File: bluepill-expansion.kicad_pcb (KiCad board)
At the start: 2 copper layers, 90.9 x 73.2 mm, 39 parts, among them J1 SENSE_A, J10 ENCODERS, J11 LS2, J12 I/O 3V3, J13 DIGITAL_PWR, J2 SENSE_B, J3 POWER_DC, J4 MOTDC1, J5 MOTDC2, J6 I2C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

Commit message: cambiosEmma
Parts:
- removed C5, C7: 0.1uF, Capacitor_THT:C_Disc_D7.5mm_W2.5mm_P5.00mm
- added T1: miTornillo, miTornillo:M3, F.Cu at (189.1, 55.8)
- added T2: miTornillo, miTornillo:M3, F.Cu at (103.9, 123.1)
- added T3: miTornillo, miTornillo:M3, F.Cu at (104.1, 55.8)
- added T4: miTornillo, miTornillo:M3, F.Cu at (189.1, 123.1)
- moved J13 7.94 mm to (118.7, 58.4)
- moved J10 6.33 mm to (152.1, 58.3)
- moved J2 5.29 mm to (157.2, 61.7)
- moved R2 5.29 mm to (182.6, 60.5)
- moved J6 2.88 mm to (112.5, 119.4)
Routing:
- net VCC: track 123.3 -> 113.6 mm
- net ENC2_Q: track 28.8 -> 35.3 mm
- net GND: track 364.9 -> 359.5 mm
- net ENC2_D: track 31.0 -> 35.4 mm
- net ENC1_D: track 41.1 -> 45.1 mm
- net ENC1_Q: track 38.7 -> 42.0 mm
- net +5V: track 255.3 -> 252.2 mm, vias 2 -> 3
- net /PB5: track 72.9 -> 70.4 mm
- net ENA: track 22.8 -> 25.1 mm
- net SENSE_B: track 15.0 -> 12.7 mm
- net +3V3: track 87.8 -> 89.9 mm
- net SCL: track 13.5 -> 11.6 mm
- net SDA: track 13.5 -> 11.6 mm
- net UARTRX: track 22.7 -> 20.9 mm
- net MOT4: track 46.6 -> 45.2 mm
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
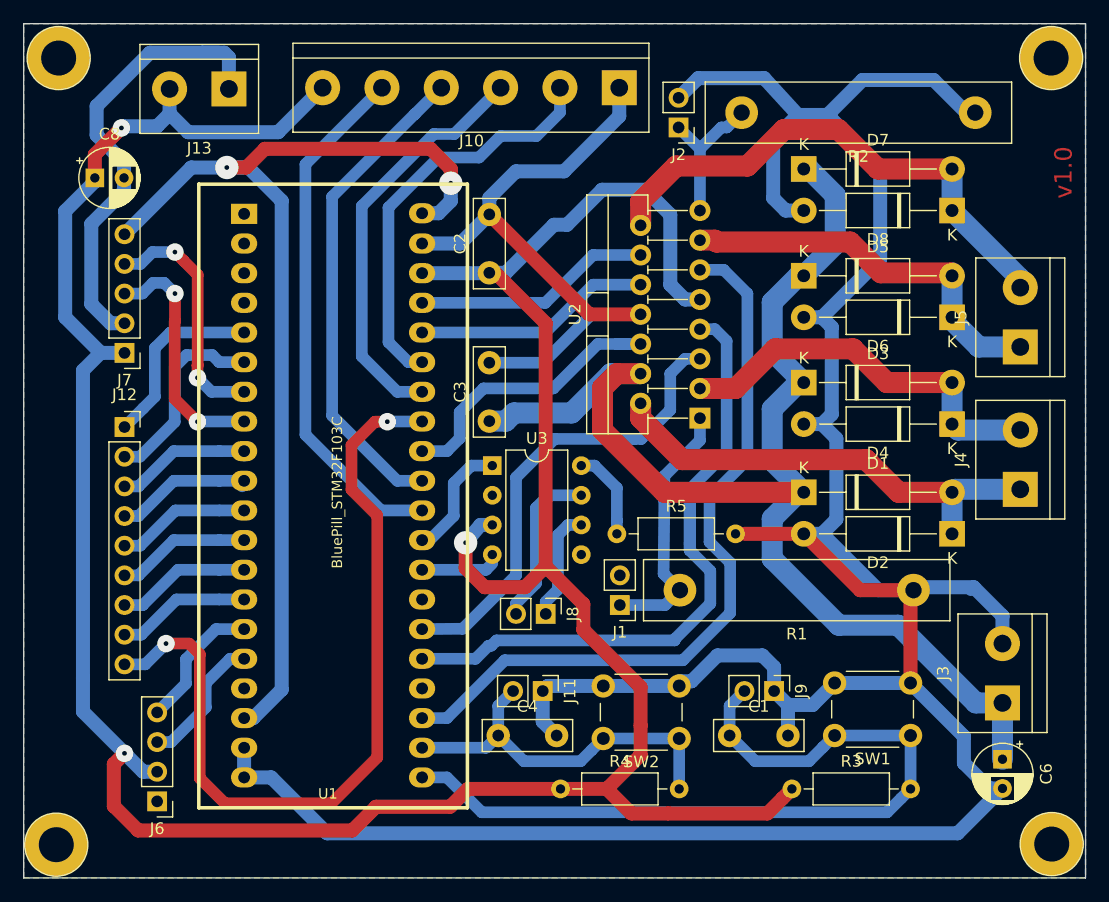
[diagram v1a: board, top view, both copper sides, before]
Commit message: CAN R 120
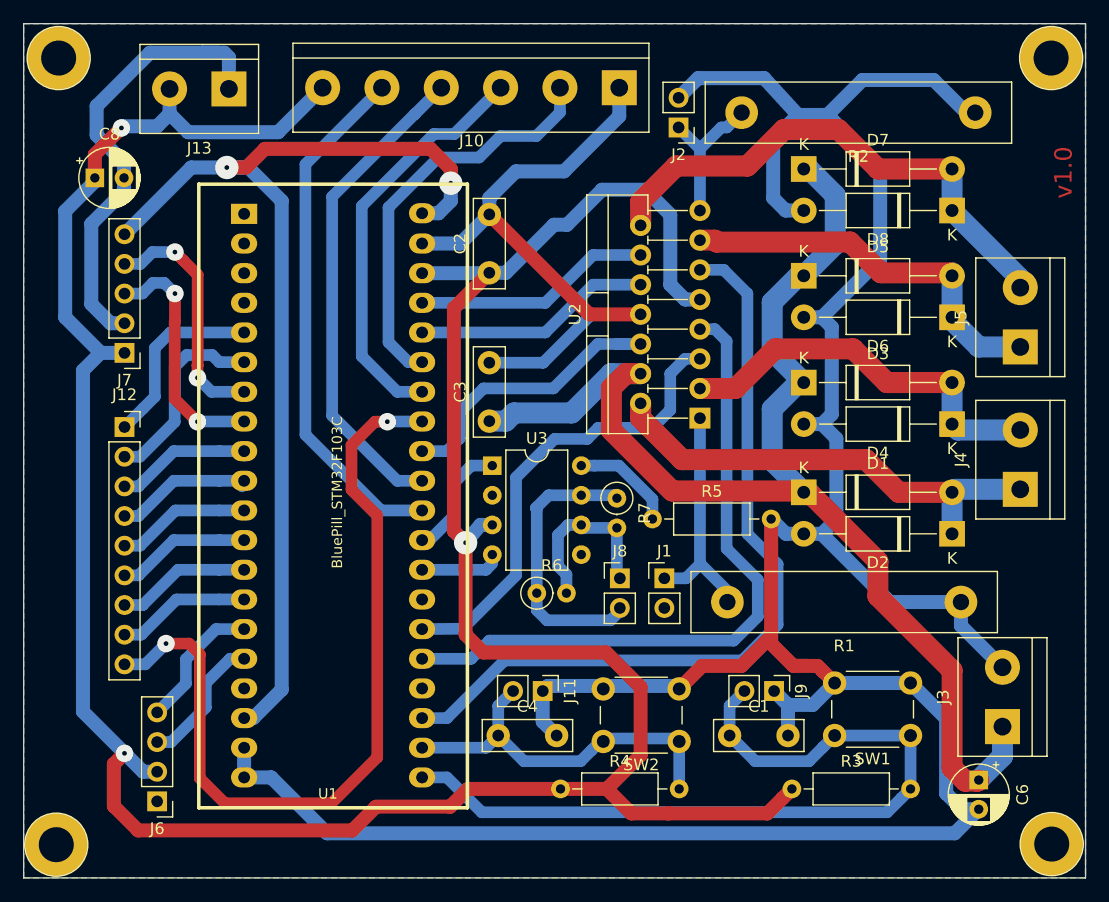
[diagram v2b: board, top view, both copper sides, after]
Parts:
- added R6: 120, Resistor_THT:R_Axial_DIN0207_L6.3mm_D2.5mm_P2.54mm_Vertical, F.Cu at (145.0, 101.6)
- added R7: 120, Resistor_THT:R_Axial_DIN0207_L6.3mm_D2.5mm_P2.54mm_Vertical, F.Cu at (151.9, 93.5)
- moved J8 7.04 mm to (152.1, 100.3), turned to 0 degrees
- moved J1 4.44 mm to (156.0, 100.3), turned to 0 degrees
- moved R1 4.19 mm to (181.4, 102.4)
- moved R5 3.30 mm to (154.9, 95.2)
- moved C6 2.70 mm to (182.9, 117.6)
- moved J3 2.03 mm to (184.9, 113.0)
- moved SW2 0.25 mm to (157.2, 114.3)
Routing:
- net GND: track 359.5 -> 349.3 mm
- net /CANH: track 14.1 -> 24.1 mm
- net /CANL: track 9.55 -> 15.7 mm
- net ENB: track 64.4 -> 68.1 mm
- net PWM2: track 59.3 -> 57.7 mm
- net +5V: track 252.2 -> 250.6 mm
- net SENSE_A: track 22.2 -> 21.0 mm
- net Net-(R5-Pad1): track 7.77 -> 8.98 mm
- net VCC: track 113.6 -> 112.6 mm

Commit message: cambios Emma para enviar a fabricar, orden bus can
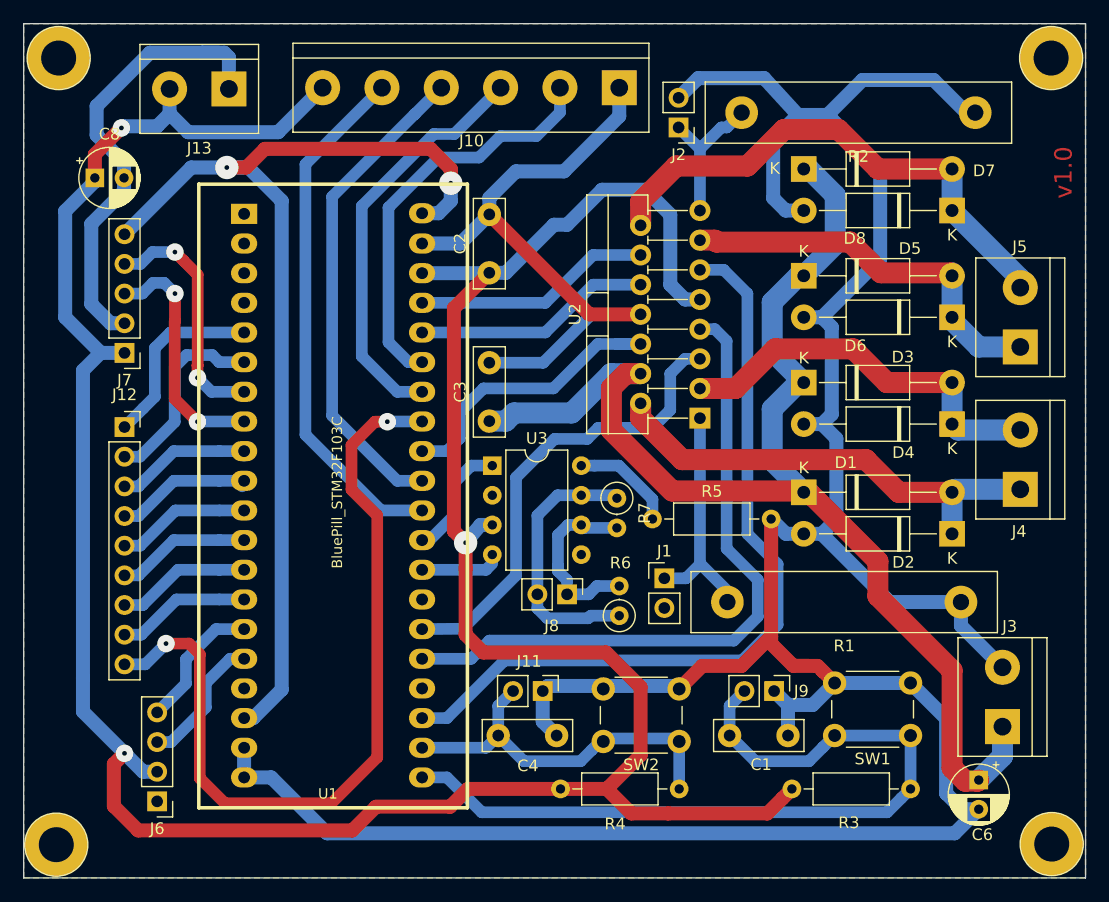
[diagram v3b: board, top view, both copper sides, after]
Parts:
- moved R6 7.32 mm to (152.1, 103.5), turned to 90 degrees
- moved J8 4.72 mm to (147.6, 101.7), turned to 270 degrees
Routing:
- net /CANH: track 24.1 -> 23.0 mm
